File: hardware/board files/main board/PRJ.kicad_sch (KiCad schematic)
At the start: 24 parts, among them J1 Strain Gauge, J2 Programmer, J3 KLIPPER, U1 HX717, U2 ATtiny202-SS, U3 AMS1117-3.3

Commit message: overhauled main board, updated credits
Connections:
- net UDPI renamed UPDI
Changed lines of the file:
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@@
     )
   )
-  (global_label "UDPI" (shape input) (at 52.07 68.58 0) (fields_autoplaced)
+  (global_label "UPDI" (shape input) (at 52.07 68.58 0) (fields_autoplaced)
     (effects (font (size 1.27 1.27)) (justify left))
     (property "Intersheetrefs" "${INTERSHEET_REFS}" (at 59.5305 68.58 0)
@@
     )
   )
-  (global_label "UDPI" (shape input) (at 33.655 34.925 0) (fields_autoplaced)
+  (global_label "UPDI" (shape input) (at 33.655 34.925 0) (fields_autoplaced)
     (effects (font (size 1.27 1.27)) (justify left))
     (property "Intersheetrefs" "${INTERSHEET_REFS}" (at 41.1155 34.925 0)
@@
     (pin "2")
     (instances
-      (project "loaddeez"
+      (project "PRJ"
         (path "/a8a69bae-b90a-439b-a99b-122d08f0220a"
           (reference "C5") (unit 1)
@@
     (pin "1")
     (instances
-      (project "loaddeez"
+      (project "PRJ"
         (path "/a8a69bae-b90a-439b-a99b-122d08f0220a"
           (reference "#PWR027") (unit 1)
@@
     (pin "2")
     (instances
-      (project "loaddeez"
+      (project "PRJ"
         (path "/a8a69bae-b90a-439b-a99b-122d08f0220a"
           (reference "C2") (unit 1)
@@
     (pin "9")
     (instances
-      (project "loaddeez"
+      (project "PRJ"
         (path "/a8a69bae-b90a-439b-a99b-122d08f0220a"
           (reference "U1") (unit 1)
@@
     (pin "2")
     (instances
-      (project "loaddeez"
+      (project "PRJ"
         (path "/a8a69bae-b90a-439b-a99b-122d08f0220a"
           (reference "C9") (unit 1)
@@
     (pin "1")
     (instances
-      (project "loaddeez"
+      (project "PRJ"
         (path "/a8a69bae-b90a-439b-a99b-122d08f0220a"
           (reference "#PWR03") (unit 1)
@@
     (pin "1")
     (instances
-      (project "loaddeez"
+      (project "PRJ"
         (path "/a8a69bae-b90a-439b-a99b-122d08f0220a"
           (reference "#PWR014") (unit 1)
@@
     (pin "2")
     (instances
-      (project "loaddeez"
+      (project "PRJ"
         (path "/a8a69bae-b90a-439b-a99b-122d08f0220a"
           (reference "J2") (unit 1)
@@
     (pin "2")
     (instances
-      (project "loaddeez"
+      (project "PRJ"
         (path "/a8a69bae-b90a-439b-a99b-122d08f0220a"
           (reference "C1") (unit 1)
@@
     (pin "8")
     (instances
-      (project "loaddeez"
+      (project "PRJ"
         (path "/a8a69bae-b90a-439b-a99b-122d08f0220a"
           (reference "U2") (unit 1)
@@
     (pin "1")
     (instances
-      (project "loaddeez"
+      (project "PRJ"
         (path "/a8a69bae-b90a-439b-a99b-122d08f0220a"
           (reference "#PWR021") (unit 1)
@@
     (pin "2")
     (instances
-      (project "loaddeez"
+      (project "PRJ"
         (path "/a8a69bae-b90a-439b-a99b-122d08f0220a"
           (reference "R10") (unit 1)
@@
     (pin "4")
     (instances
-      (project "loaddeez"
+      (project "PRJ"
         (path "/a8a69bae-b90a-439b-a99b-122d08f0220a"
           (reference "J3") (unit 1)
@@
     (pin "2")
     (instances
-      (project "loaddeez"
+      (project "PRJ"
         (path "/a8a69bae-b90a-439b-a99b-122d08f0220a"
           (reference "R9") (unit 1)
@@
     (pin "2")
     (instances
-      (project "loaddeez"
+      (project "PRJ"
         (path "/a8a69bae-b90a-439b-a99b-122d08f0220a"
           (reference "C8") (unit 1)
@@
     (pin "3")
     (instances
-      (project "loaddeez"
+      (project "PRJ"
         (path "/a8a69bae-b90a-439b-a99b-122d08f0220a"
           (reference "U3") (unit 1)
@@
     (pin "1")
     (instances
-      (project "loaddeez"
+      (project "PRJ"
         (path "/a8a69bae-b90a-439b-a99b-122d08f0220a"
           (reference "#PWR011") (unit 1)
@@
     (pin "1")
     (instances
-      (project "loaddeez"
+      (project "PRJ"
         (path "/a8a69bae-b90a-439b-a99b-122d08f0220a"
           (reference "#PWR02") (unit 1)
@@
     (pin "1")
     (instances
-      (project "loaddeez"
+      (project "PRJ"
         (path "/a8a69bae-b90a-439b-a99b-122d08f0220a"
           (reference "#PWR01") (unit 1)
@@
     (pin "1")
     (instances
-      (project "loaddeez"
+      (project "PRJ"
         (path "/a8a69bae-b90a-439b-a99b-122d08f0220a"
           (reference "#PWR08") (unit 1)
@@
     (pin "2")
     (instances
-      (project "loaddeez"
+      (project "PRJ"
         (path "/a8a69bae-b90a-439b-a99b-122d08f0220a"
           (reference "C3") (unit 1)
@@
     (pin "1")
     (instances
-      (project "loaddeez"
+      (project "PRJ"
         (path "/a8a69bae-b90a-439b-a99b-122d08f0220a"
           (reference "#PWR012") (unit 1)
@@
     (pin "1")
     (instances
-      (project "loaddeez"
+      (project "PRJ"
         (path "/a8a69bae-b90a-439b-a99b-122d08f0220a"
           (reference "#PWR06") (unit 1)
@@
     (pin "1")
     (instances
-      (project "loaddeez"
+      (project "PRJ"
         (path "/a8a69bae-b90a-439b-a99b-122d08f0220a"
           (reference "#PWR016") (unit 1)
@@
     (pin "2")
     (instances
-      (project "loaddeez"
+      (project "PRJ"
         (path "/a8a69bae-b90a-439b-a99b-122d08f0220a"
           (reference "R4") (unit 1)
@@
     (pin "2")
     (instances
-      (project "loaddeez"
+      (project "PRJ"
         (path "/a8a69bae-b90a-439b-a99b-122d08f0220a"
           (reference "R2") (unit 1)
@@
     (pin "2")
     (instances
-      (project "loaddeez"
+      (project "PRJ"
         (path "/a8a69bae-b90a-439b-a99b-122d08f0220a"
           (reference "C7") (unit 1)
@@
     (pin "2")
     (instances
-      (project "loaddeez"
+      (project "PRJ"
         (path "/a8a69bae-b90a-439b-a99b-122d08f0220a"
           (reference "R3") (unit 1)
@@
     (pin "2")
     (instances
-      (project "loaddeez"
+      (project "PRJ"
         (path "/a8a69bae-b90a-439b-a99b-122d08f0220a"
           (reference "D1") (unit 1)
@@
     (pin "2")
     (instances
-      (project "loaddeez"
+      (project "PRJ"
         (path "/a8a69bae-b90a-439b-a99b-122d08f0220a"
           (reference "C4") (unit 1)
@@
     (pin "1")
     (instances
-      (project "loaddeez"
+      (project "PRJ"
         (path "/a8a69bae-b90a-439b-a99b-122d08f0220a"
           (reference "#PWR015") (unit 1)
@@
     (pin "1")
     (instances
-      (project "loaddeez"
+      (project "PRJ"
         (path "/a8a69bae-b90a-439b-a99b-122d08f0220a"
           (reference "#PWR026") (unit 1)
@@
     (pin "1")
     (instances
-      (project "loaddeez"
+      (project "PRJ"
         (path "/a8a69bae-b90a-439b-a99b-122d08f0220a"
           (reference "#PWR028") (unit 1)
@@
     (pin "1")
     (instances
-      (project "loaddeez"
+      (project "PRJ"
         (path "/a8a69bae-b90a-439b-a99b-122d08f0220a"
           (reference "#PWR07") (unit 1)
@@
     (pin "1")
     (instances
-      (project "loaddeez"
+      (project "PRJ"
         (path "/a8a69bae-b90a-439b-a99b-122d08f0220a"
           (reference "#PWR022") (unit 1)
@@
     (pin "1")
     (instances
-      (project "loaddeez"
+      (project "PRJ"
         (path "/a8a69bae-b90a-439b-a99b-122d08f0220a"
           (reference "#PWR030") (unit 1)
@@
     (pin "4")
     (instances
-      (project "loaddeez"
+      (project "PRJ"
         (path "/a8a69bae-b90a-439b-a99b-122d08f0220a"
           (reference "J1") (unit 1)
@@
     (pin "1")
     (instances
-      (project "loaddeez"
+      (project "PRJ"
         (path "/a8a69bae-b90a-439b-a99b-122d08f0220a"
           (reference "#PWR029") (unit 1)
@@
     (pin "1")
     (instances
-      (project "loaddeez"
+      (project "PRJ"
         (path "/a8a69bae-b90a-439b-a99b-122d08f0220a"
           (reference "#PWR020") (unit 1)
@@
     (pin "1")
     (instances
-      (project "loaddeez"
+      (project "PRJ"
         (path "/a8a69bae-b90a-439b-a99b-122d08f0220a"
           (reference "#PWR010") (unit 1)
@@
     (pin "2")
     (instances
-      (project "loaddeez"
+      (project "PRJ"
         (path "/a8a69bae-b90a-439b-a99b-122d08f0220a"
           (reference "R1") (unit 1)
@@
     (pin "1")
     (instances
-      (project "loaddeez"
+      (project "PRJ"
         (path "/a8a69bae-b90a-439b-a99b-122d08f0220a"
           (reference "H1") (unit 1)
@@
     (pin "1")
     (instances
-      (project "loaddeez"
+      (project "PRJ"
         (path "/a8a69bae-b90a-439b-a99b-122d08f0220a"
           (reference "#PWR019") (unit 1)
@@
     (pin "1")
     (instances
-      (project "loaddeez"
+      (project "PRJ"
         (path "/a8a69bae-b90a-439b-a99b-122d08f0220a"
           (reference "#PWR025") (unit 1)
@@
     (pin "1")
     (instances
-      (project "loaddeez"
+      (project "PRJ"
         (path "/a8a69bae-b90a-439b-a99b-122d08f0220a"
           (reference "#PWR04") (unit 1)
@@
     (pin "2")
     (instances
-      (project "loaddeez"
+      (project "PRJ"
         (path "/a8a69bae-b90a-439b-a99b-122d08f0220a"
           (reference "C6") (unit 1)
@@
     (pin "1")
     (instances
-      (project "loaddeez"
+      (project "PRJ"
         (path "/a8a69bae-b90a-439b-a99b-122d08f0220a"
           (reference "#PWR05") (unit 1)
@@
     (pin "1")
     (instances
-      (project "loaddeez"
+      (project "PRJ"
         (path "/a8a69bae-b90a-439b-a99b-122d08f0220a"
           (reference "H2") (unit 1)
@@
     (pin "1")
     (instances
-      (project "loaddeez"
+      (project "PRJ"
         (path "/a8a69bae-b90a-439b-a99b-122d08f0220a"
           (reference "#PWR013") (unit 1)
@@
     (pin "1")
     (instances
-      (project "loaddeez"
+      (project "PRJ"
         (path "/a8a69bae-b90a-439b-a99b-122d08f0220a"
           (reference "#PWR09") (unit 1)

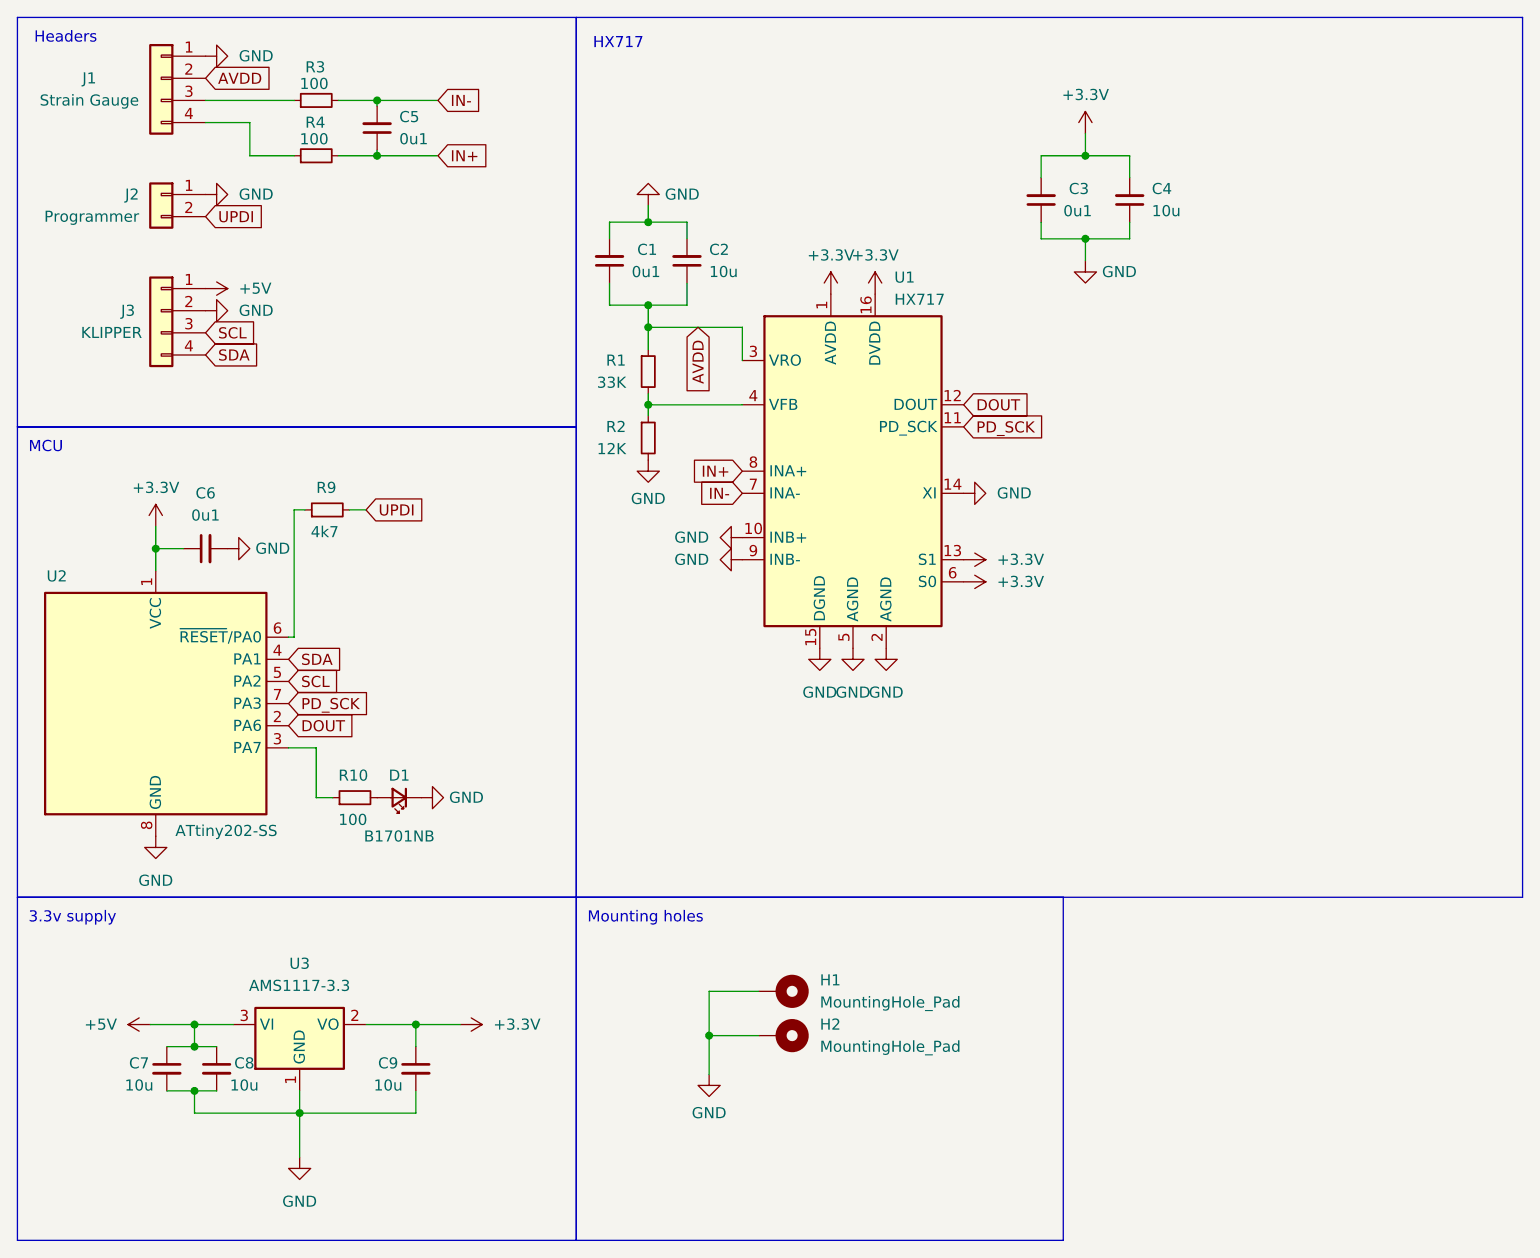
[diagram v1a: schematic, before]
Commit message: added initial prototype of production unit with attiny202 and hx71708
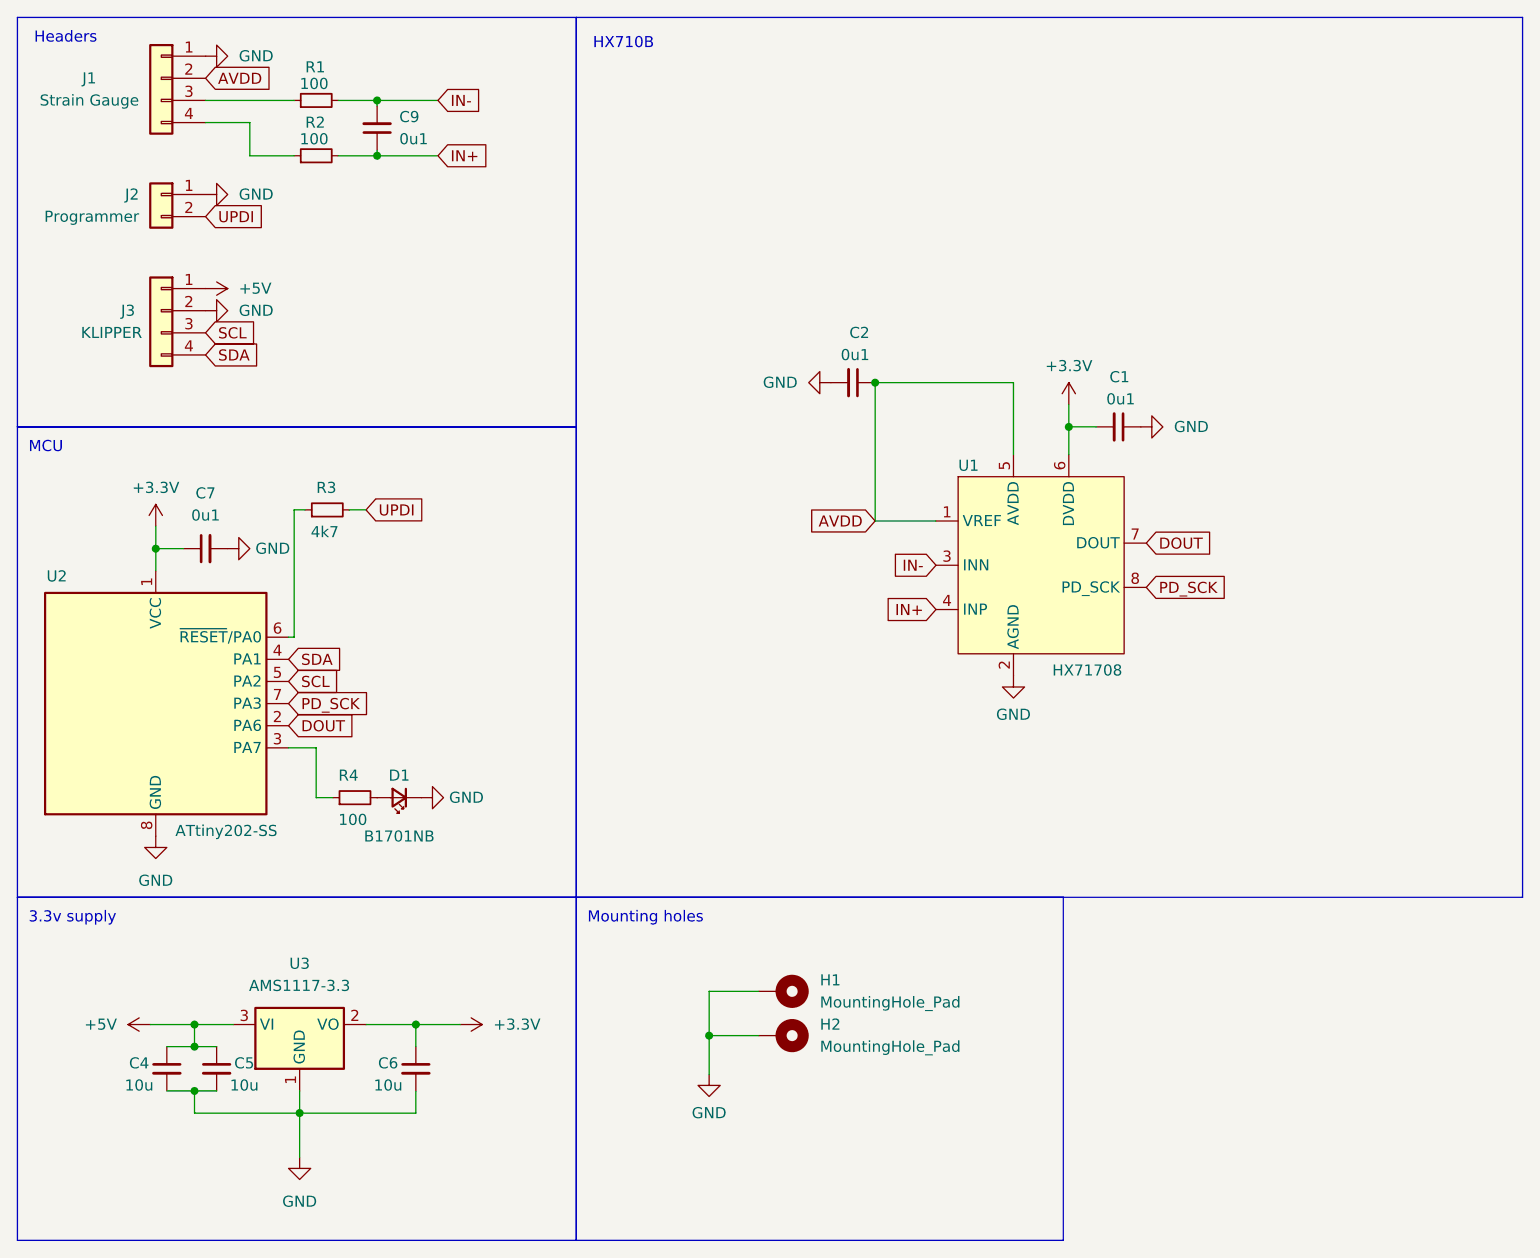
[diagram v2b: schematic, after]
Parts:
- removed C1: 0u1, Capacitor_SMD:C_0805_2012Metric_Pad1.18x1.45mm_HandSolder, symbol Device:C_Small
- removed C4: 10u, Capacitor_SMD:C_0805_2012Metric_Pad1.18x1.45mm_HandSolder, symbol Device:C_Small
- removed R1: 33K, Resistor_SMD:R_0805_2012Metric_Pad1.20x1.40mm_HandSolder, symbol Device:R_Small
- removed R2: 12K, Resistor_SMD:R_0805_2012Metric_Pad1.20x1.40mm_HandSolder, symbol Device:R_Small
- removed U1: HX717, Package_SO:SOP-16_3.9x9.9mm_P1.27mm, symbol custom:HX717
- added U1: HX71708, Package_SO:SOIC-8_3.9x4.9mm_P1.27mm, symbol hx710b:HX71708
- C1: renamed from C3; footprint Capacitor_SMD:C_0805_2012Metric_Pad1.18x1.45mm_HandSolder -> Capacitor_SMD:C_0402_1005Metric
- C2: value 10u -> 0u1; footprint Capacitor_SMD:C_0805_2012Metric_Pad1.18x1.45mm_HandSolder -> Capacitor_SMD:C_0402_1005Metric
- C4: renamed from C7; footprint Capacitor_SMD:C_0805_2012Metric_Pad1.18x1.45mm_HandSolder -> Capacitor_SMD:C_0402_1005Metric
- C5: renamed from C8; footprint Capacitor_SMD:C_0805_2012Metric_Pad1.18x1.45mm_HandSolder -> Capacitor_SMD:C_0402_1005Metric
- C6: renamed from C9; footprint Capacitor_SMD:C_0805_2012Metric_Pad1.18x1.45mm_HandSolder -> Capacitor_SMD:C_0402_1005Metric
- C7: renamed from C6; footprint Capacitor_SMD:C_0805_2012Metric_Pad1.18x1.45mm_HandSolder -> Capacitor_SMD:C_0402_1005Metric
- C9: renamed from C5; footprint Capacitor_SMD:C_0805_2012Metric_Pad1.18x1.45mm_HandSolder -> Capacitor_SMD:C_0402_1005Metric
- D1: footprint LED_SMD:LED_0805_2012Metric_Pad1.15x1.40mm_HandSolder -> LED_SMD:LED_0402_1005Metric
- R1: renamed from R3; footprint Resistor_SMD:R_0805_2012Metric_Pad1.20x1.40mm_HandSolder -> Resistor_SMD:R_0402_1005Metric
- R2: renamed from R4; footprint Resistor_SMD:R_0805_2012Metric_Pad1.20x1.40mm_HandSolder -> Resistor_SMD:R_0402_1005Metric
- R3: renamed from R9; footprint Resistor_SMD:R_0805_2012Metric_Pad1.20x1.40mm_HandSolder -> Resistor_SMD:R_0402_1005Metric
- R4: renamed from R10; footprint Resistor_SMD:R_0805_2012Metric_Pad1.20x1.40mm_HandSolder -> Resistor_SMD:R_0402_1005Metric
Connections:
- net +3.3V: now also U1.6 (DVDD)
- net AVDD: now also U1.1 (VREF), U1.5 (AVDD)
- net DOUT: now also U1.7 (DOUT)
- net GND: now also U1.2 (AGND)
- net IN+: now also U1.4 (INP)
- net IN-: now also U1.3 (INN)
- net PD_SCK: now also U1.8 (PD_SCK)
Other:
- note added: "HX710B"
- note removed: "HX717"
- moved on the sheet: C1
